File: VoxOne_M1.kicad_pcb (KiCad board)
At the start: 2 copper layers, 100 x 100 mm, 81 parts, among them J101 ARK 5V / GND, J301 AUDIO OUT: 1=L 2=GND 3=R, J401 BT LEFT INNER / USB DOWN, J402 BT RIGHT INNER / USB DOWN, J501 I2C: VCC GND SDA SCL, J502 SPI: VCC GND SCK MOSI CS DC R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, J601 INPUT: S1 S2 KEY GND, J603 AMP: EN_OC MUTE_OC GND, Q101 FDD6685 DPAK, Q401 MMBT3904 / reset OC, Q503 MMBT3904 BL drive, Q504 AO3401A BL high-side, Q601 MMBT3904 EN OC, Q602 MMBT3904 MUTE OC, U101 AMS1117-3.3 (UMW), U201 ESP32-S3 DevKitC-1 N16R8 (*), U301 PCM5102A MODULE / JACK RIGHT, U501 SN74LVC1G17DBV, U601 DS3231 for Pi / 5 POS

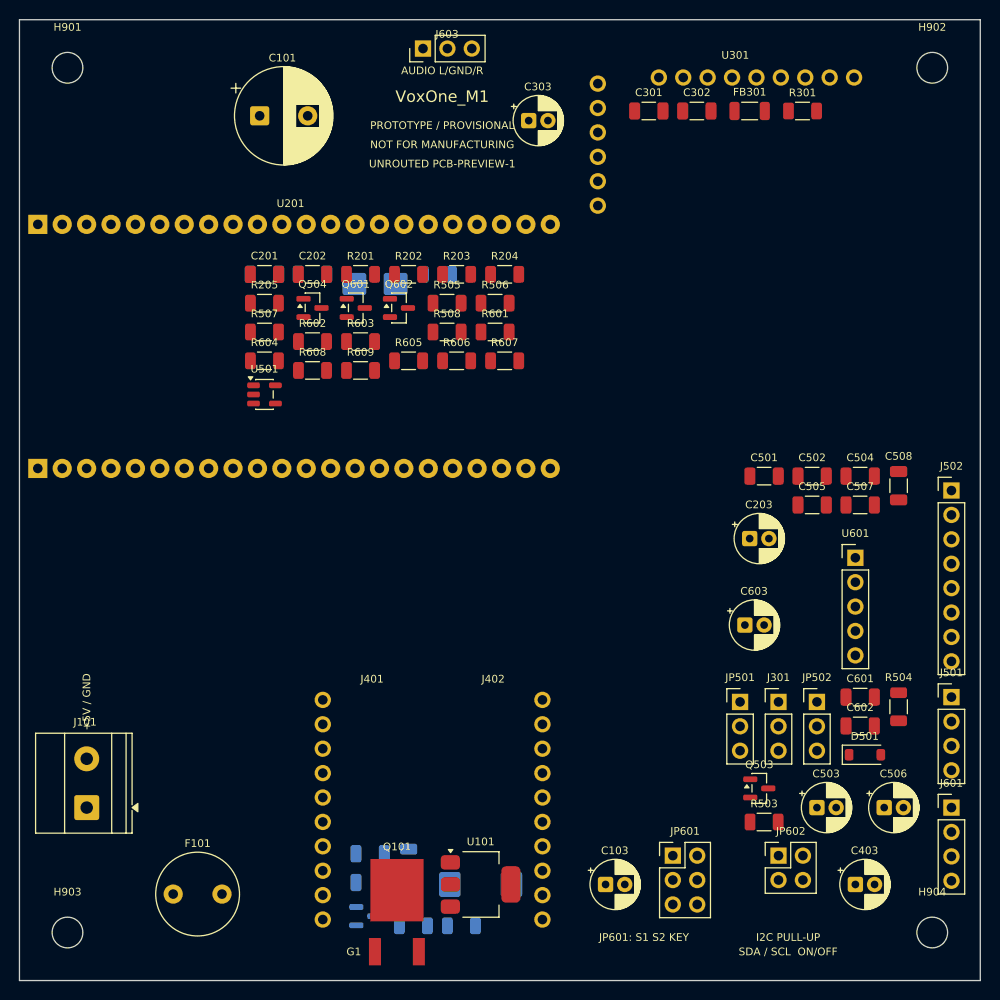
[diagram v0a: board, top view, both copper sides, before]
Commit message: PCB-LAYOUT-2: all-top provisional placement and full verification
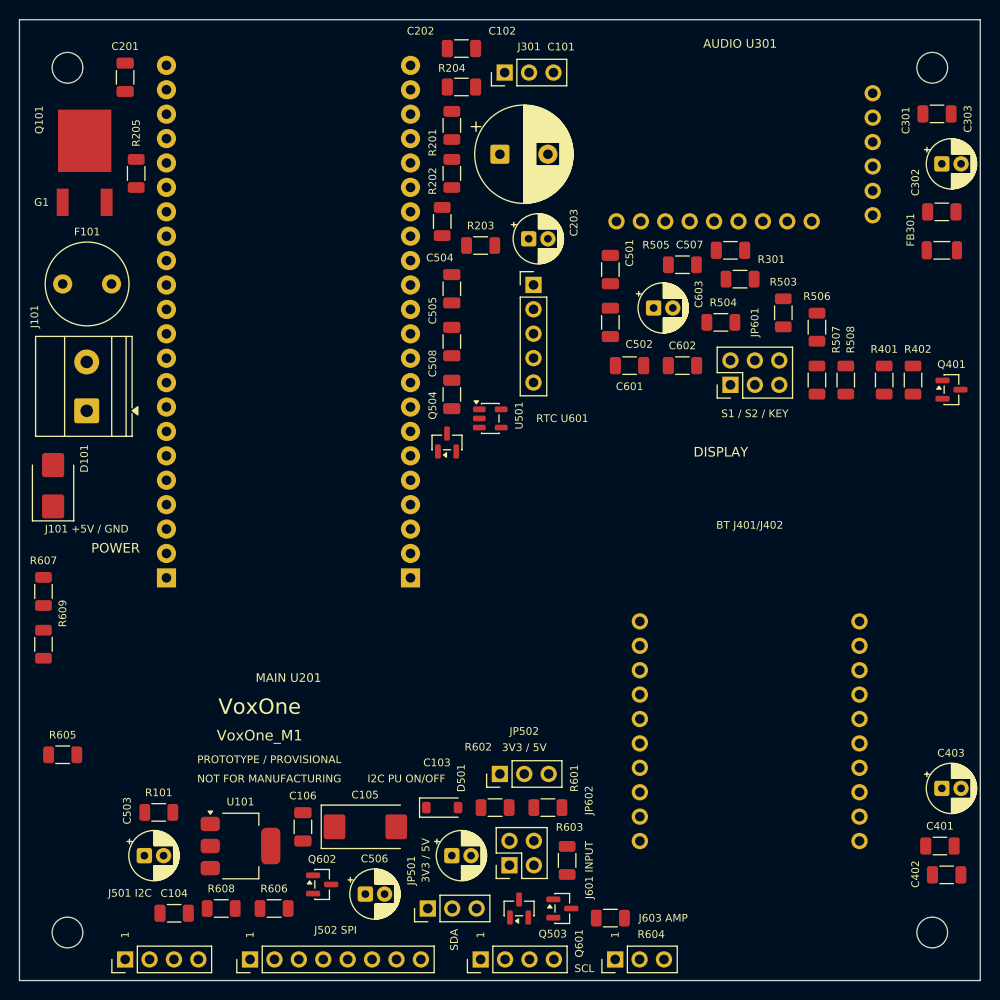
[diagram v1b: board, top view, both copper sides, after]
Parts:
- C102, C104, C105, C106, C401, C402, D101, Q401, R101, R401, R402: moved to F.Cu
- moved J603 96.9 mm to (112.0, 147.8)
- moved J501 90.2 mm to (61.0, 147.8), turned to 90 degrees
- moved J502 87.8 mm to (74.0, 147.8), turned to 90 degrees
- moved Q101 84.5 mm to (54.5, 69.0)
- moved Q401 82.0 mm to (147.0, 88.5)
- moved C102 81.0 mm to (96.0, 57.0), turned to 0 degrees
- moved R401 75.0 mm to (140.0, 87.5), turned to 90 degrees
- moved R402 73.7 mm to (143.0, 87.5), turned to 90 degrees
- moved J301 71.4 mm to (100.5, 55.5), turned to 90 degrees
- moved C503 70.2 mm to (63.0, 137.0)
- moved R604 68.3 mm to (111.5, 143.5)
- moved C104 67.2 mm to (66.1, 143.0)
- moved Q601 66.1 mm to (106.5, 142.5)
- moved F101 64.5 mm to (54.5, 77.5)
- moved R101 63.1 mm to (64.5, 132.5)
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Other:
- board text added: "1"
- board text added: "3V3 / 5V"
- board text added: "AUDIO U301"
- board text added: "BT / PROVISIONAL"
- board text added: "BT J401/J402"
- board text added: "DAC / PROVISIONAL"
- board text added: "DISPLAY"
- board text added: "I2C PU ON/OFF"
- board text added: "J101 +5V / GND"
- board text added: "J501 I2C"
- board text added: "J502 SPI"
- board text added: "J601 INPUT"
- board text added: "J603 AMP"
- board text added: "MAIN / PROVISIONAL"
- board text added: "MAIN U201"
- board text added: "PCB-LAYOUT-2 | PROTOTYPE / PROVISIONAL - NOT FOR MANUFACTURING"
- board text added: "POWER"
- board text added: "RTC / PROVISIONAL"
- board text added: "RTC U601"
- board text added: "S1 / S2 / KEY"
- board text added: "SCL"
- board text added: "SDA"
- board text added: "VoxOne"
- board text removed: "+5V / GND"
- board text removed: "AUDIO L/GND/R"
- board text removed: "BT ANT NO COPPER"
- board text removed: "I2C PULL-UP"
- board text removed: "JP601: S1 S2 KEY"
- board text removed: "MAIN ANT NO COPPER"
- board text removed: "RTC 13.4 REF"
- board text removed: "SDA / SCL ON/OFF"
- board text removed: "UNROUTED PCB-PREVIEW-1"

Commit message: PCB-LAYOUT-3: redesign placement from user reference and verify native KiCad
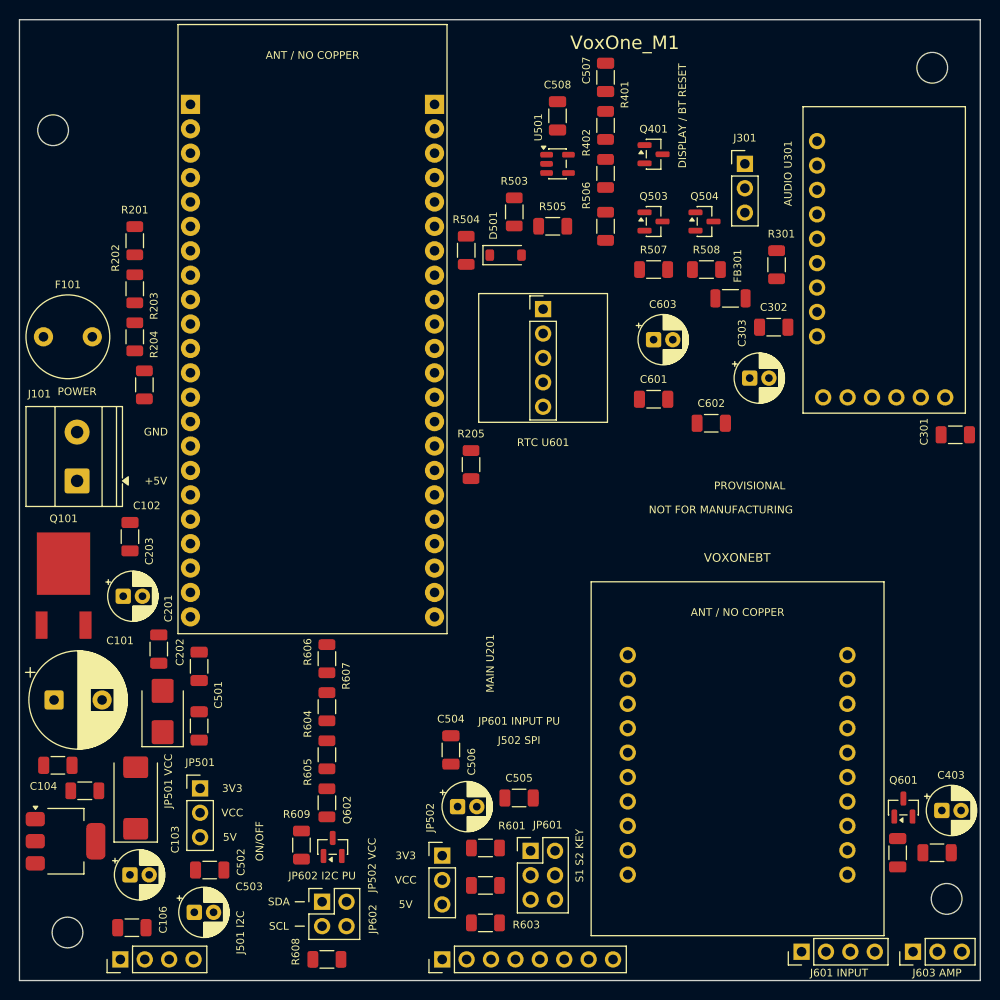
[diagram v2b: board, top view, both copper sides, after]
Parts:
- moved C101 73.3 mm to (53.6, 120.8)
- moved Q503 72.9 mm to (116.0, 71.0), turned to 0 degrees
- moved C502 70.6 mm to (69.8, 138.5), turned to 0 degrees
- moved C202 69.9 mm to (68.7, 117.3), turned to 90 degrees
- moved C501 63.9 mm to (68.7, 123.5)
- moved C201 59.6 mm to (64.5, 115.5)
- moved U201 58.9 mm to (66.5, 56.9), turned to 0 degrees
- moved C102 58.1 mm to (61.5, 103.8), turned to 90 degrees
- moved D501 57.9 mm to (100.6, 74.5)
- moved C203 56.3 mm to (60.8, 110.0)
- moved JP601 52.8 mm to (103.2, 136.5), turned to 0 degrees
- moved C505 48.0 mm to (102.0, 131.0), turned to 0 degrees
- moved C504 48.0 mm to (94.9, 126.0)
- moved R205 46.2 mm to (97.0, 96.3)
- moved Q101 44.1 mm to (52.3, 113.0)
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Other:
- board text added: "+5V"
- board text added: "3V3"
- board text added: "5V"
- board text added: "ANT / NO COPPER"
- board text added: "DISPLAY / BT RESET"
- board text added: "GND"
- board text added: "JACK_DAC_PLUG"
- board text added: "JP501 VCC"
- board text added: "JP501 see pin pairs / ON=shunt OFF=open"
- board text added: "JP502 VCC"
- board text added: "JP502 see pin pairs / ON=shunt OFF=open"
- board text added: "JP601 INPUT PU"
- board text added: "JP601 see pin pairs / ON=shunt OFF=open"
- board text added: "JP602 I2C PU"
- board text added: "JP602 see pin pairs / ON=shunt OFF=open"
- board text added: "KEY"
- board text added: "ON/OFF"
- board text added: "PROTOTYPE / PROVISIONAL - NOT FOR MANUFACTURING"
- board text added: "PROVISIONAL"
- board text added: "S1"
- board text added: "S1 S2 KEY"
- board text added: "S2"
- board text added: "USB_BT_PLUG"
- board text added: "USB_MAIN_1_CABLE"
- board text added: "USB_MAIN_1_PLUG"
- board text added: "USB_MAIN_2_CABLE"
- board text added: "USB_MAIN_2_PLUG"
- board text added: "VCC"
- board text added: "VOXONEBT"
- board text added: "VoxOne_M1 / PCB-LAYOUT-3"
- board text removed: "1"
- board text removed: "3V3 / 5V"
- board text removed: "BT J401/J402"
- board text removed: "DISPLAY"
- board text removed: "I2C PU ON/OFF"
- board text removed: "J101 +5V / GND"
- board text removed: "PCB-LAYOUT-2 | PROTOTYPE / PROVISIONAL - NOT FOR MANUFACTURING"
- board text removed: "PROTOTYPE / PROVISIONAL"
- board text removed: "S1 / S2 / KEY"
- board text removed: "VoxOne"
